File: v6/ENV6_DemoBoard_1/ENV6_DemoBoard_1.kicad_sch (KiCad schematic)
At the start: 0 parts

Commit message: ENV6 (test): Changes after first review
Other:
- note added: "Extension Board"
- note added: "Main Board"

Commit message: Changes after second rev of ENV6 test
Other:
- added sheet Connector (connector.kicad_sch)
- sheet MCU ports: added none; removed VCC_MCU
- sheet Peripherals ports: added none; removed VCC_MCU
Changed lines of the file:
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@@
 	(wire
 		(pts
-			(xy 171.45 35.56) (xy 179.07 35.56)
+			(xy 55.88 34.29) (xy 63.5 34.29)
 		)
 		(stroke
@@
 	(wire
 		(pts
-			(xy 63.5 33.02) (xy 68.58 33.02)
+			(xy 55.88 39.37) (xy 63.5 39.37)
 		)
 		(stroke
@@
 	(wire
 		(pts
-			(xy 171.45 40.64) (xy 179.07 40.64)
+			(xy 55.88 36.83) (xy 63.5 36.83)
 		)
 		(stroke
@@
 	(wire
 		(pts
-			(xy 171.45 38.1) (xy 179.07 38.1)
-		)
-		(stroke
-			(width 0)
-			(type default)
-		)
-	)
-	(wire
-		(pts
-			(xy 171.45 33.02) (xy 179.07 33.02)
-		)
-		(stroke
-			(width 0)
-			(type default)
-		)
-	)
-	(wire
-		(pts
-			(xy 171.45 46.99) (xy 179.07 46.99)
+			(xy 55.88 31.75) (xy 63.5 31.75)
 		)
 		(stroke
@@
 	)
 	(label "1V1"
-		(at 179.07 38.1 180)
+		(at 63.5 36.83 180)
 		(effects
 			(font
@@
 	)
 	(label "3V3"
-		(at 68.58 33.02 180)
+		(at 63.5 31.75 180)
 		(effects
 			(font
@@
 		)
 	)
-	(label "3V3"
-		(at 179.07 33.02 180)
+	(label "0V8"
+		(at 63.5 39.37 180)
 		(effects
 			(font
@@
 		)
 	)
-	(label "3V3"
-		(at 179.07 46.99 180)
+	(label "1V8"
+		(at 63.5 34.29 180)
 		(effects
 			(font
@@
 		)
 	)
-	(label "0V8"
-		(at 179.07 40.64 180)
-		(effects
-			(font
-				(size 1.27 1.27)
-			)
-			(justify right bottom)
-		)
-	)
-	(label "1V8"
-		(at 179.07 35.56 180)
-		(effects
-			(font
-				(size 1.27 1.27)
-			)
-			(justify right bottom)
-		)
-	)
 	(sheet
-		(at 139.7 30.48)
+		(at 24.13 29.21)
 		(size 31.75 26.035)
 		(exclude_from_sim no)
@@
 		)
 		(property "Sheetname" "Peripherals"
-			(at 139.7 29.7684 0)
+			(at 24.13 28.4984 0)
 			(effects
 				(font
@@
 		)
 		(property "Sheetfile" "Peripherals.kicad_sch"
-			(at 139.7 57.0996 0)
+			(at 24.13 55.8296 0)
 			(effects
 				(font
@@
 		)
 		(pin "V4" output
-			(at 171.45 40.64 0)
+			(at 55.88 39.37 0)
 			(effects
 				(font
@@
 			)
 		)
-		(pin "VCC_MCU" input
-			(at 171.45 46.99 0)
+		(pin "V2" output
+			(at 55.88 34.29 0)
 			(effects
 				(font
@@
 			)
 		)
-		(pin "V2" output
-			(at 171.45 35.56 0)
+		(pin "V3" output
+			(at 55.88 36.83 0)
 			(effects
 				(font
@@
 			)
 		)
-		(pin "V3" output
-			(at 171.45 38.1 0)
+		(pin "V1" output
+			(at 55.88 31.75 0)
 			(effects
 				(font
@@
 			)
 		)
-		(pin "V1" output
-			(at 171.45 33.02 0)
-			(effects
-				(font
-					(size 1.27 1.27)
-				)
-				(justify right)
-			)
-		)
 		(instances
 			(project "ENV6_DemoBoard_1"
 				(path "/c353698e-fca1-4ed3-95bc-4f5142868012"
-					(page "4")
+					(page "2")
 				)
 			)
@@
 	)
 	(sheet
-		(at 85.09 29.845)
+		(at 67.945 29.21)
 		(size 32.385 26.035)
 		(exclude_from_sim no)
@@
 		)
 		(property "Sheetname" "Power"
-			(at 85.09 29.1334 0)
+			(at 67.945 28.4984 0)
 			(effects
 				(font
@@
 		)
 		(property "Sheetfile" "Power.kicad_sch"
-			(at 85.09 56.4646 0)
+			(at 67.945 55.8296 0)
 			(effects
 				(font
@@
 	)
 	(sheet
-		(at 31.115 29.845)
+		(at 151.765 29.845)
+		(size 33.02 25.4)
+		(exclude_from_sim no)
+		(in_bom yes)
+		(on_board yes)
+		(dnp no)
+		(fields_autoplaced yes)
+		(stroke
+			(width 0.1524)
+			(type solid)
+		)
+		(fill
+			(color 0 0 0 0.0000)
+		)
+		(property "Sheetname" "Connector"
+			(at 151.765 29.1334 0)
+			(effects
+				(font
+					(size 1.27 1.27)
+				)
+				(justify left bottom)
+			)
+		)
+		(property "Sheetfile" "connector.kicad_sch"
+			(at 151.765 55.8296 0)
+			(effects
+				(font
+					(size 1.27 1.27)
+				)
+				(justify left top)
+			)
+		)
+		(instances
+			(project "ENV6_DemoBoard_1"
+				(path "/c353698e-fca1-4ed3-95bc-4f5142868012"
+					(page "4")
+				)
+			)
+		)
+	)
+	(sheet
+		(at 109.22 29.21)
 		(size 32.385 26.67)
 		(exclude_from_sim no)
@@
 		)
 		(property "Sheetname" "MCU"
-			(at 31.115 29.1334 0)
+			(at 109.22 28.4984 0)
 			(effects
 				(font
@@
 		)
 		(property "Sheetfile" "MCU.kicad_sch"
-			(at 31.115 57.0996 0)
+			(at 109.22 56.4646 0)
 			(effects
 				(font
@@
 			)
 		)
-		(pin "VCC_MCU" input
-			(at 63.5 33.02 0)
-			(effects
-				(font
-					(size 1.27 1.27)
-				)
-				(justify right)
-			)
-		)
 		(instances
 			(project "ENV6_DemoBoard_1"
 				(path "/c353698e-fca1-4ed3-95bc-4f5142868012"
-					(page "2")
+					(page "4")
 				)
 			)

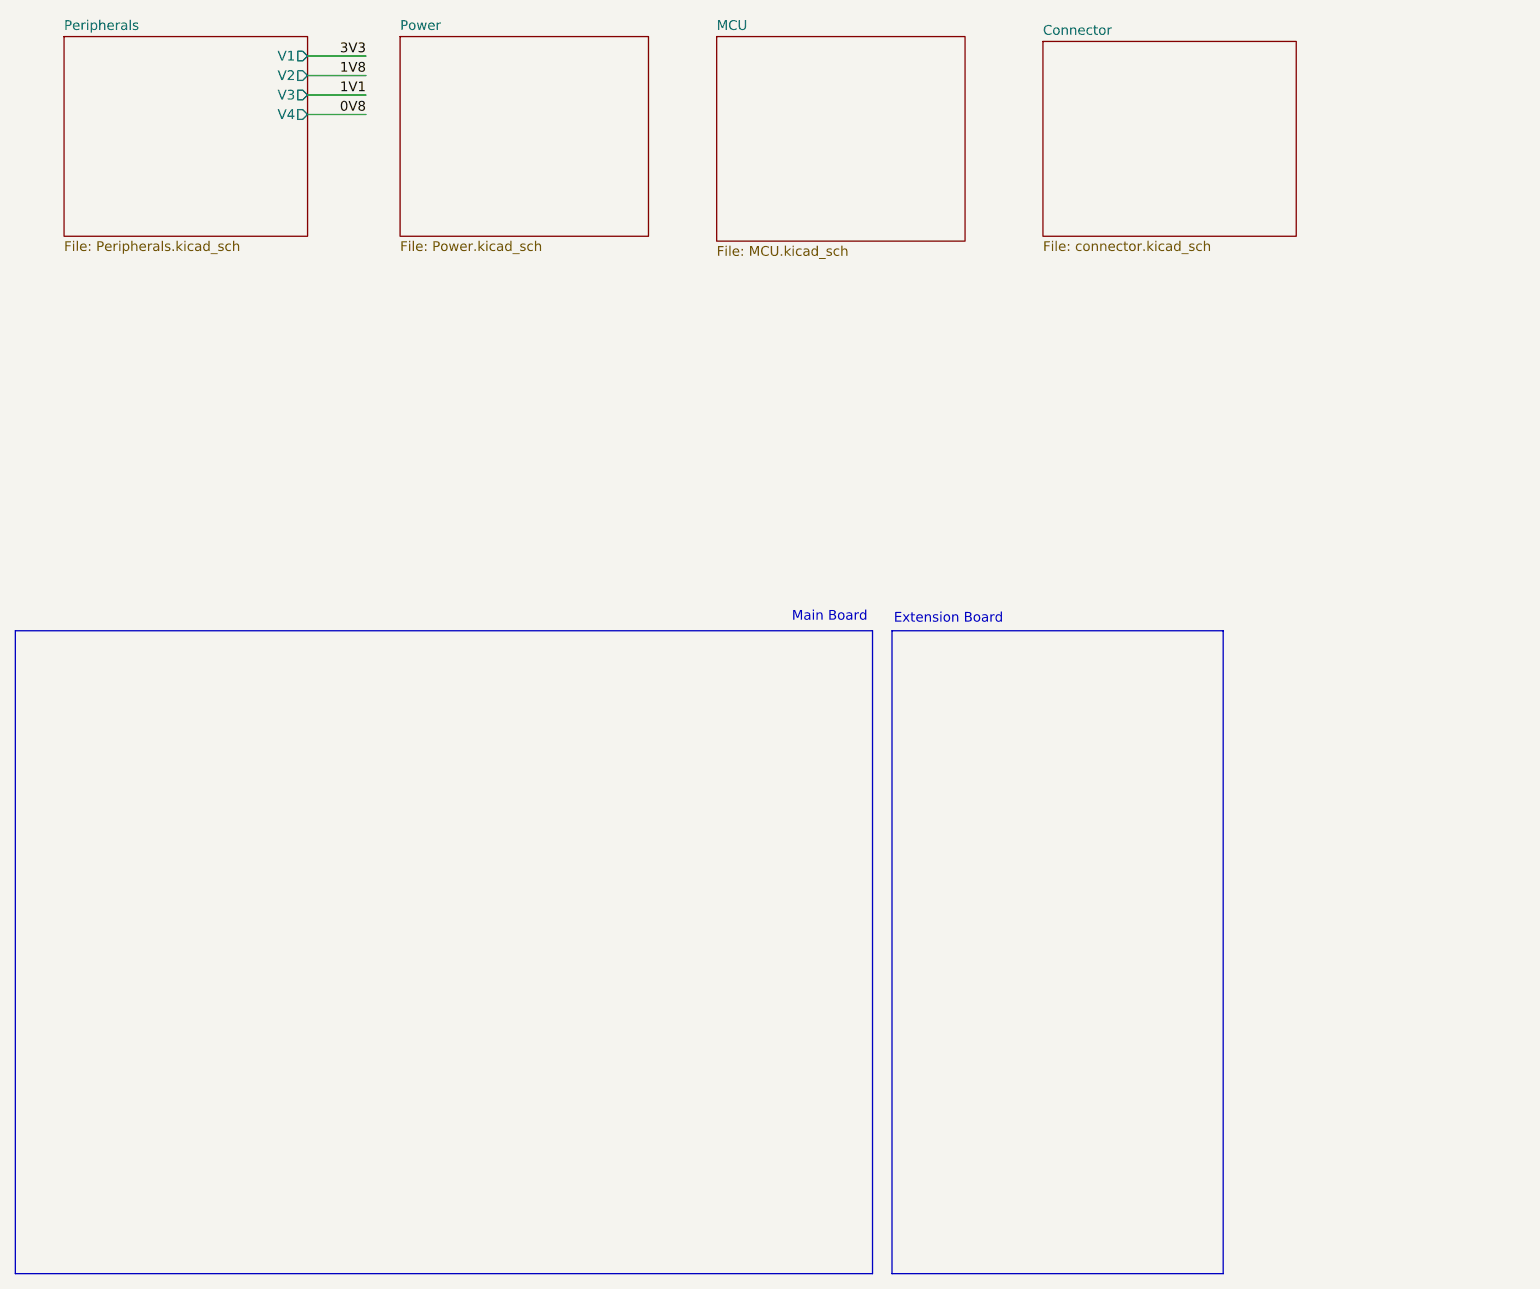
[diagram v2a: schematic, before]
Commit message: update Demoboard and add GateMateA11 board
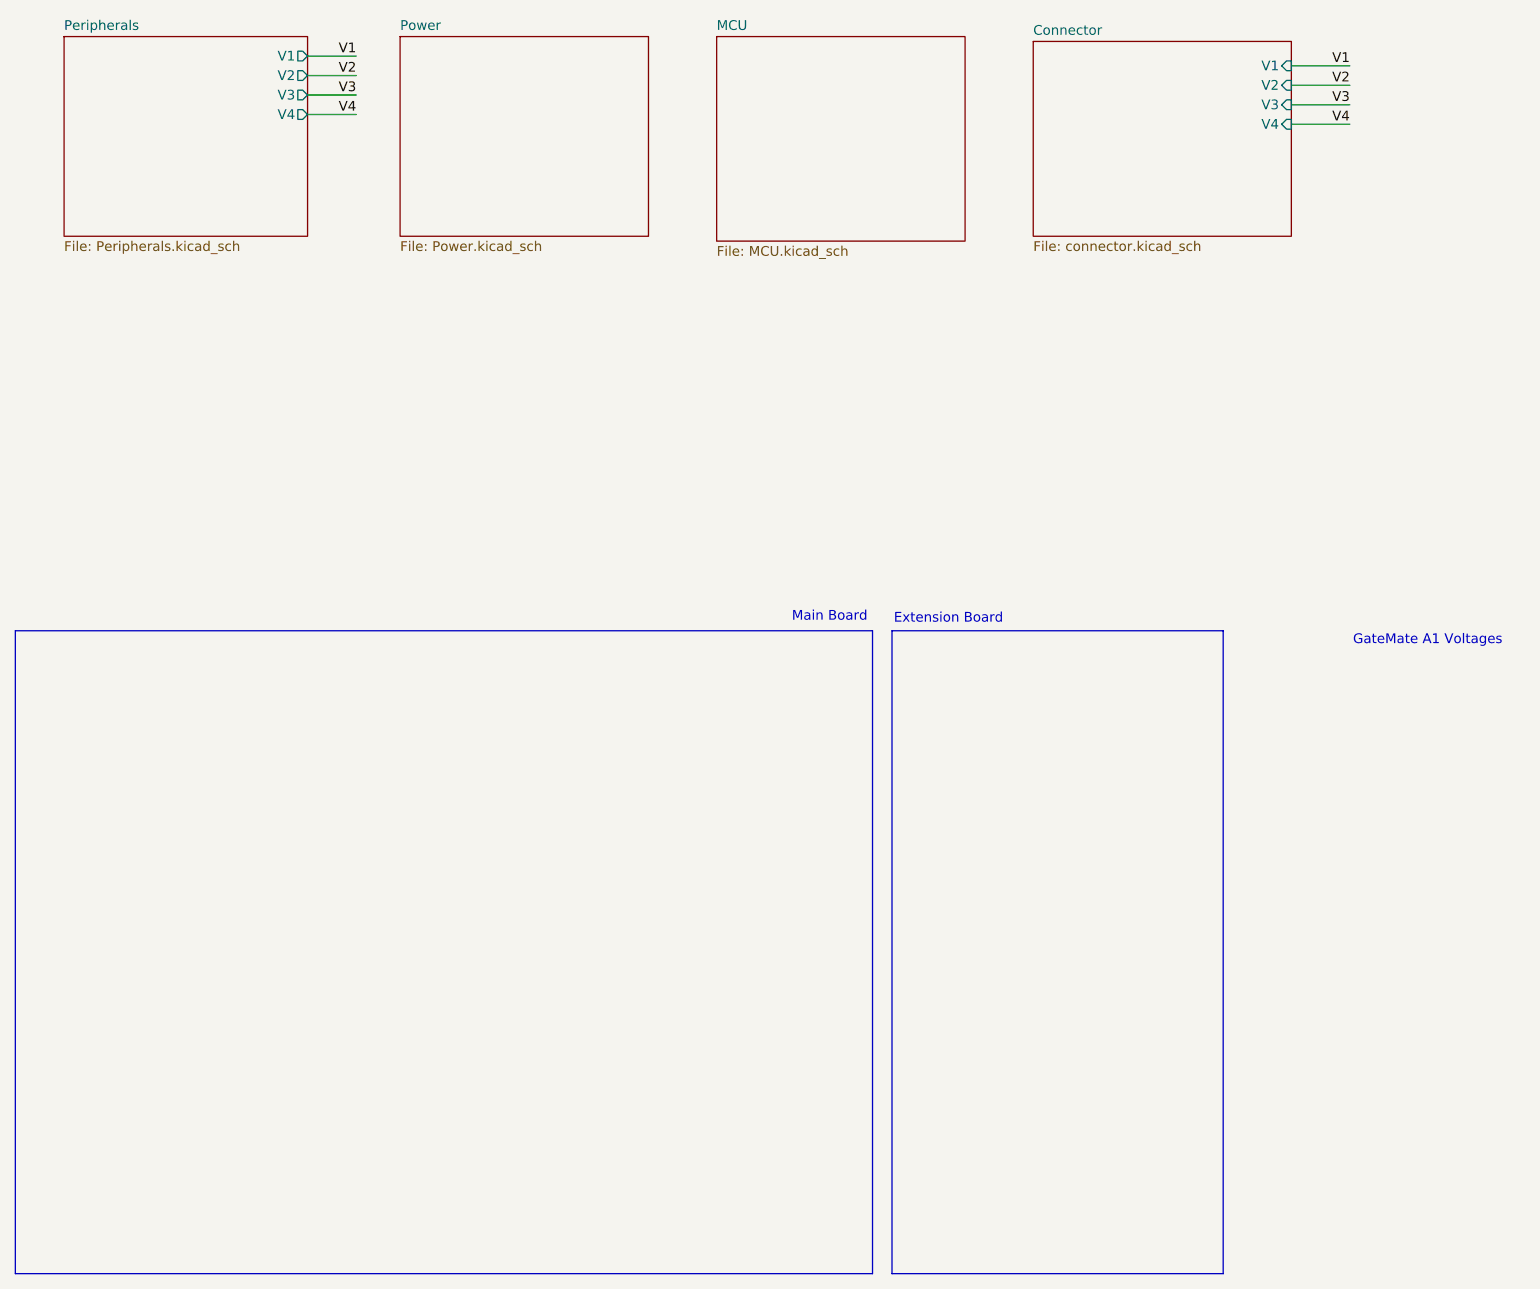
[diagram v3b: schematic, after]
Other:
- sheet Connector ports: added V1, V2, V3, V4; removed none
- note added: "GateMate A1 Voltages"
